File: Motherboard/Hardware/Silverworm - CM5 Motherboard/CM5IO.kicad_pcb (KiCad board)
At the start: 4 copper layers, 160 x 90 mm, 81 parts, among them J10 690-019-298-412, J11 USB_C_Receptacle_USB2.0, J12 USB3_A, J14 JST_SHBM04B-SRSS-TB, J16 Conn_01x22_Female, J2 Conn_02x07_Odd_Even, J22 690-019-298-412, J3 Conn_01x03, J4 Bus_M.2_Socket_M, J5 Conn_01x22_Female, J6 THD-02-R, J7 Micro_SD_Card_Det, J8 THD-20-R, J9 THD-02-R, SW1 Right angle Tact button, U1 TPD4EUSB30, U12 RT9742SNGV, U18 RT9742GGJ5, U2 TPD4EUSB30, U3 MagJack-A70-112-331N126, U6 AP22653W6, U7 ASEK-32.768KHZ-L-R-T, U8 AP3441SHE-7B

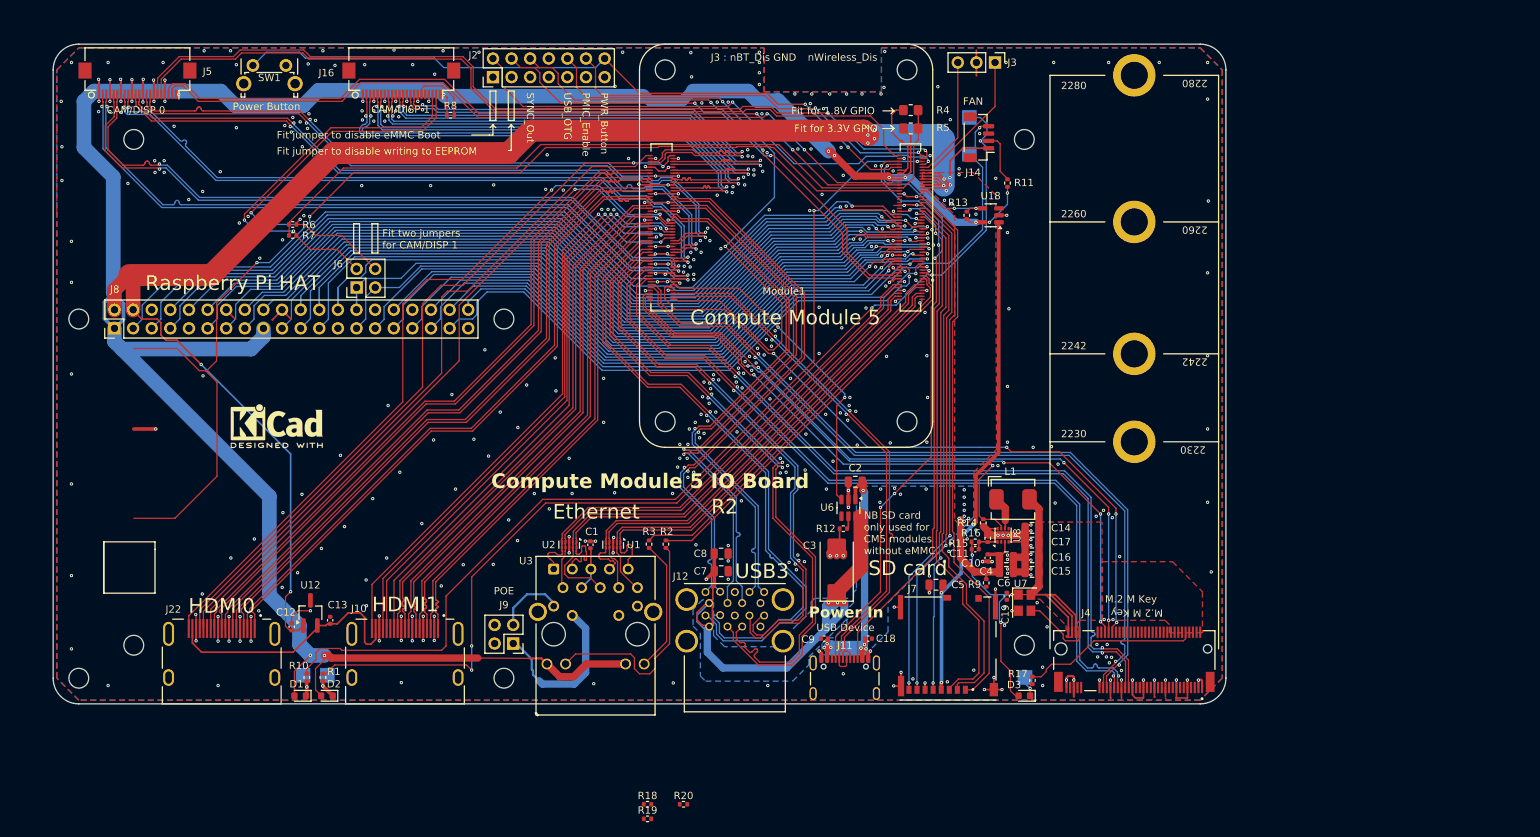
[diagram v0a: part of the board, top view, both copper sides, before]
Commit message: Added footprints and board connectors
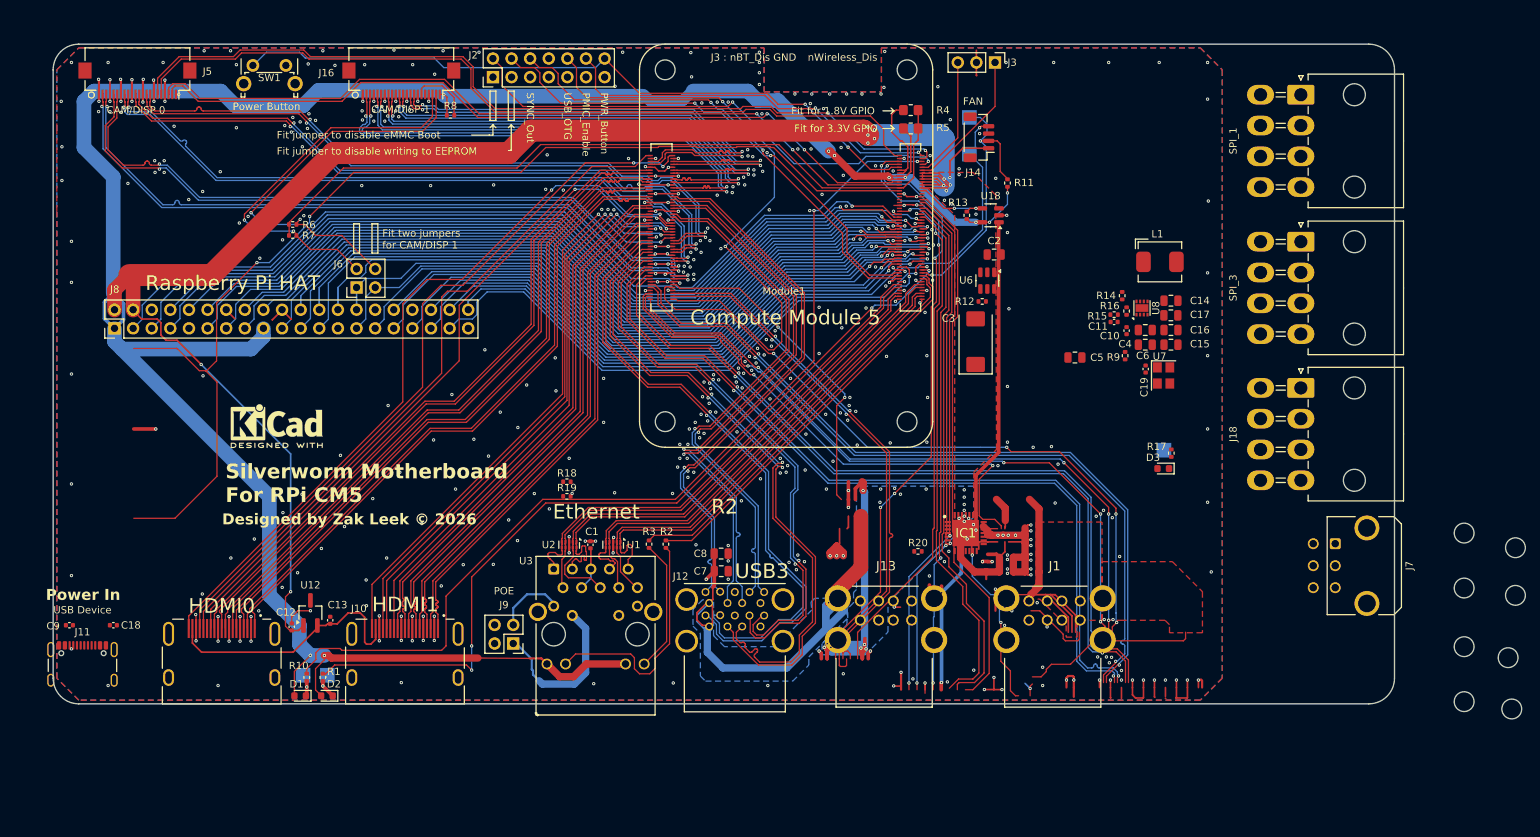
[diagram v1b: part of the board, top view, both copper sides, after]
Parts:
- removed J4: Bus_M.2_Socket_M, CM5IO:M.2 M Key socket
- added IC1: CY7C65632-28LTXC, CM5IO:QFN50P500X500X80-29N-D, F.Cu at (203.5, 136.7)
- added J1: USB_A_Stacked, CM5IO:57876171, F.Cu at (215.5, 152.2)
- added J13: USB_A_Stacked, CM5IO:57876171, F.Cu at (192.5, 152.2)
- added J18: Minifit 2x4, Connector_Molex:Molex_Mini-Fit_Jr_5569-08A2_2x04_P4.20mm_Horizontal, F.Cu at (249.2, 116.9)
- added SPI_1: Minifit 2x4, Connector_Molex:Molex_Mini-Fit_Jr_5569-08A2_2x04_P4.20mm_Horizontal, F.Cu at (249.2, 76.9)
- added SPI_3: Minifit 2x4, Connector_Molex:Molex_Mini-Fit_Jr_5569-08A2_2x04_P4.20mm_Horizontal, F.Cu at (249.2, 97.0)
- J7: value Micro_SD_Card_Det -> Microfit 6-pin; footprint CM5IO:SDCARD_MOLEX_503398-1892 -> Connector_Molex:Molex_Micro-Fit_3.0_43045-0621_2x03-1MP_P3.00mm_Horizontal
- moved H3 199.6 mm to (278.5, 145.2)
- moved H7 191.5 mm to (271.5, 144.2), turned to 90 degrees
- moved H2 190.0 mm to (271.5, 136.7), turned to 90 degrees
- moved H1 187.5 mm to (277.5, 153.7)
- moved H5 141.5 mm to (278.5, 138.7)
- moved H4 137.6 mm to (278.0, 160.7)
- moved J11 104.0 mm to (83.0, 155.7)
- moved C18 103.0 mm to (87.2, 149.3)
- moved C9 103.0 mm to (81.2, 149.3)
- moved H6 91.6 mm to (271.5, 152.2), turned to 90 degrees
- moved H8 60.5 mm to (271.5, 159.7), turned to 90 degrees
- moved J7 54.7 mm to (253.9, 138.2), turned to -90 degrees
- moved R20 47.0 mm to (197.0, 139.2)
- moved R18 45.4 mm to (149.1, 129.7)
- moved R19 45.4 mm to (149.1, 131.7)
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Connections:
- J7 pad 1: /CM5_GPIO ( Ethernet, GPIO, SDCARD)/SD_DAT2 -> GND
- J7 pad 2: /CM5_GPIO ( Ethernet, GPIO, SDCARD)/SD_DAT3 -> /CM5_GPIO ( Ethernet, GPIO, SDCARD)/5V0
- J7 pad 3: /CM5_GPIO ( Ethernet, GPIO, SDCARD)/SD_CMD -> /CM5_GPIO ( Ethernet, GPIO, SDCARD)/SCL
- J7 pad 4: /CM5_GPIO ( Ethernet, GPIO, SDCARD)/SD_PWR -> /CM5_GPIO ( Ethernet, GPIO, SDCARD)/SDA
- J7 pad 5: /CM5_GPIO ( Ethernet, GPIO, SDCARD)/SD_CLK -> /CM5_GPIO ( Ethernet, GPIO, SDCARD)/12VDC
- Module1 pad 102: /CM5_HighSpeed/PCIE_nCLKREQ -> unconnected-(Module1B-PCIe_nCLKREQ-Pad102)
- Module1 pad 104: /CM5_HighSpeed/PCIE_nWAKE -> unconnected-(Module1B-PCIE_nWAKE-Pad104)
- Module1 pad 106: /CM5_HighSpeed/PCIE_PWR_EN -> unconnected-(Module1B-PCIE_PWR_EN-Pad106)
- Module1 pad 109: /CM5_HighSpeed/PCIE_nRST -> unconnected-(Module1B-PCIe_nRST-Pad109)
- Module1 pad 110: /CM5_HighSpeed/PCIE_CLK_P -> unconnected-(Module1B-PCIe_CLK_P-Pad110)
- Module1 pad 112: /CM5_HighSpeed/PCIE_CLK_N -> unconnected-(Module1B-PCIe_CLK_N-Pad112)
- Module1 pad 116: /CM5_HighSpeed/PCIE_RX_P -> unconnected-(Module1B-PCIe_RX_P-Pad116)
- Module1 pad 118: /CM5_HighSpeed/PCIE_RX_N -> unconnected-(Module1B-PCIe_RX_N-Pad118)
- Module1 pad 122: /CM5_HighSpeed/PCIE_TX_P -> unconnected-(Module1B-PCIe_TX_P-Pad122)
- Module1 pad 124: /CM5_HighSpeed/PCIE_TX_N -> unconnected-(Module1B-PCIe_TX_N-Pad124)
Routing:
- net (no net): track 143.6 -> 0.00 mm, vias 4 -> 0
- net unconnected-(Module1B-PCIe_TX_N-Pad124): track 0.00 -> 109.5 mm, vias 0 -> 2
- net /CM5_HighSpeed/PCIE_TX_N: track 109.5 -> 0.00 mm, vias 2 -> 0
- net unconnected-(Module1B-PCIe_TX_P-Pad122): track 0.00 -> 109.5 mm, vias 0 -> 2
- net /CM5_HighSpeed/PCIE_TX_P: track 109.5 -> 0.00 mm, vias 2 -> 0
- net unconnected-(Module1B-PCIe_RX_N-Pad118): track 0.00 -> 107.9 mm, vias 0 -> 2
- net /CM5_HighSpeed/PCIE_RX_N: track 107.9 -> 0.00 mm, vias 2 -> 0
- net unconnected-(Module1B-PCIe_RX_P-Pad116): track 0.00 -> 107.8 mm, vias 0 -> 2
- net /CM5_HighSpeed/PCIE_RX_P: track 107.8 -> 0.00 mm, vias 2 -> 0
- net unconnected-(Module1B-PCIe_CLK_N-Pad112): track 0.00 -> 103.8 mm, vias 0 -> 2
- net /CM5_HighSpeed/PCIE_CLK_N: track 103.8 -> 0.00 mm, vias 2 -> 0
- net unconnected-(Module1B-PCIe_CLK_P-Pad110): track 0.00 -> 103.8 mm, vias 0 -> 2
- net /CM5_HighSpeed/PCIE_CLK_P: track 103.8 -> 0.00 mm, vias 2 -> 0
- net unconnected-(Module1B-PCIe_nRST-Pad109): track 0.00 -> 93.4 mm, vias 0 -> 4
- net /CM5_HighSpeed/PCIE_nRST: track 93.4 -> 0.00 mm, vias 4 -> 0
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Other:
- board size 160 x 90 mm -> 183 x 90 mm
- board text added: "Designed by Zak Leek © 2026"
- board text added: "Silverworm Motherboard For RPi CM5"
- board text added: "Why are you loking at my bottom? ;)"
- board text removed: "Compute Module 5 IO Board"
- board text removed: "M.2 M Key"
- board text removed: "NB SD card only used for CM5 modules without eMMC"
- board text removed: "SD card"

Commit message: Layout and IO edits
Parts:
- moved C10 21.4 mm to (224.1, 130.5)
- moved C11 21.4 mm to (222.4, 129.3)
- moved C14 21.4 mm to (230.2, 126.4)
- moved C15 21.4 mm to (230.2, 132.4)
- moved C16 21.4 mm to (230.2, 130.4)
- moved C17 21.4 mm to (230.1, 128.4)
- moved C19 21.4 mm to (226.7, 135.7)
- moved C4 21.4 mm to (226.7, 130.4)
- moved C5 21.4 mm to (217.1, 134.2)
- moved C6 21.4 mm to (226.7, 132.4)
- moved D3 21.4 mm to (229.1, 149.3)
- moved R14 21.4 mm to (223.5, 125.7)
- moved R15 21.4 mm to (222.4, 128.3)
- moved R9 21.4 mm to (223.9, 133.9)
- moved TP1 21.4 mm to (229.2, 146.8)
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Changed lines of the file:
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@@
 	(footprint "Capacitor_SMD:C_0805_2012Metric"
 		(layer "F.Cu")
-		(at 218.4 112.75 180)
+		(at 217.05 134.15 180)
 		(descr "Capacitor SMD 0805 (2012 Metric), square (rectangular) end terminal, IPC_7351 nominal, (Body size source: IPC-SM-782 page 76, https://www.pcb-3d.com/wordpress/wp-content/uploads/ipc-sm-782a_amendment_1_and_2.pdf, https://docs.google.com/spreadsheets/d/1BsfQQcO9C6DZCsRaXUlFlo91Tg2WpOkGARC1WS5S8t0/edit?usp=sharing), generated with kicad-footprint-generator")
 		(tags "capacitor")
@@
 	(footprint "LED_SMD:LED_0603_1608Metric"
 		(layer "F.Cu")
-		(at 230.45 127.9 180)
+		(at 229.1 149.3 180)
 		(descr "LED SMD 0603 (1608 Metric), square (rectangular) end terminal, IPC_7351 nominal, (Body size source: http://www.tortai-tech.com/upload/download/2011102023233369053.pdf), generated with kicad-footprint-generator")
 		(tags "LED")
@@
 	(footprint "Package_DFN_QFN:DFN-8-1EP_2x2mm_P0.5mm_EP1.05x1.75mm"
 		(layer "F.Cu")
-		(at 227.55 106 90)
+		(at 226.2 127.4 90)
 		(descr "DFN8 2x2, 0.5P; CASE 506CN (see ON Semiconductor 506CN.PDF)")
 		(tags "DFN 0.5")
@@
 	(footprint "Resistor_SMD:R_0402_1005Metric"
 		(layer "F.Cu")
-		(at 225.25 112.5 -90)
+		(at 223.9 133.9 -90)
 		(descr "Resistor SMD 0402 (1005 Metric), square (rectangular) end terminal, IPC_7351 nominal, (Body size source: IPC-SM-782 page 72, https://www.pcb-3d.com/wordpress/wp-content/uploads/ipc-sm-782a_amendment_1_and_2.pdf), generated with kicad-footprint-generator")
 		(tags "resistor")
@@
 	(footprint "Capacitor_SMD:C_0805_2012Metric"
 		(layer "F.Cu")
-		(at 228 111)
+		(at 226.65 132.4)
 		(descr "Capacitor SMD 0805 (2012 Metric), square (rectangular) end terminal, IPC_7351 nominal, (Body size source: IPC-SM-782 page 76, https://www.pcb-3d.com/wordpress/wp-content/uploads/ipc-sm-782a_amendment_1_and_2.pdf, https://docs.google.com/spreadsheets/d/1BsfQQcO9C6DZCsRaXUlFlo91Tg2WpOkGARC1WS5S8t0/edit?usp=sharing), generated with kicad-footprint-generator")
 		(tags "capacitor")
@@
 	(footprint "Capacitor_SMD:C_0805_2012Metric"
 		(layer "F.Cu")
-		(at 231.5 109 180)
+		(at 230.15 130.4 180)
 		(descr "Capacitor SMD 0805 (2012 Metric), square (rectangular) end terminal, IPC_7351 nominal, (Body size source: IPC-SM-782 page 76, https://www.pcb-3d.com/wordpress/wp-content/uploads/ipc-sm-782a_amendment_1_and_2.pdf, https://docs.google.com/spreadsheets/d/1BsfQQcO9C6DZCsRaXUlFlo91Tg2WpOkGARC1WS5S8t0/edit?usp=sharing), generated with kicad-footprint-generator")
 		(tags "capacitor")
@@
 	(footprint "Capacitor_SMD:C_0402_1005Metric"
 		(layer "F.Cu")
-		(at 225.45 109.085 -90)
+		(at 224.1 130.485 -90)
 		(descr "Capacitor SMD 0402 (1005 Metric), square (rectangular) end terminal, IPC_7351 nominal, (Body size source: IPC-SM-782 page 76, https://www.pcb-3d.com/wordpress/wp-content/uploads/ipc-sm-782a_amendment_1_and_2.pdf), generated with kicad-footprint-generator")
 		(tags "capacitor")
@@
 	(footprint "Capacitor_SMD:C_0402_1005Metric"
 		(layer "F.Cu")
-		(at 223.75 107.9)
+		(at 222.4 129.3)
 		(descr "Capacitor SMD 0402 (1005 Metric), square (rectangular) end terminal, IPC_7351 nominal, (Body size source: IPC-SM-782 page 76, https://www.pcb-3d.com/wordpress/wp-content/uploads/ipc-sm-782a_amendment_1_and_2.pdf), generated with kicad-footprint-generator")
 		(tags "capacitor")
@@
 	(footprint "Capacitor_SMD:C_0805_2012Metric"
 		(layer "F.Cu")
-		(at 231.4875 107 180)
+		(at 230.1375 128.4 180)
 		(descr "Capacitor SMD 0805 (2012 Metric), square (rectangular) end terminal, IPC_7351 nominal, (Body size source: IPC-SM-782 page 76, https://www.pcb-3d.com/wordpress/wp-content/uploads/ipc-sm-782a_amendment_1_and_2.pdf, https://docs.google.com/spreadsheets/d/1BsfQQcO9C6DZCsRaXUlFlo91Tg2WpOkGARC1WS5S8t0/edit?usp=sharing), generated with kicad-footprint-generator")
 		(tags "capacitor")
@@
 	(footprint "Crystal:Crystal_SMD_3225-4Pin_3.2x2.5mm"
 		(layer "F.Cu")
-		(at 230.5 115.2 -90)
+		(at 229.15 136.6 -90)
 		(descr "SMD Crystal SERIES SMD3225/4 http://www.txccrystal.com/images/pdf/7m-accuracy.pdf, 3.2x2.5mm^2 package")
 		(tags "SMD SMT crystal")
@@
 	(footprint "Resistor_SMD:R_0402_1005Metric"
 		(layer "F.Cu")
-		(at 231.55 125.8 90)
+		(at 230.2 147.2 90)
 		(descr "Resistor SMD 0402 (1005 Metric), square (rectangular) end terminal, IPC_7351 nominal, (Body size source: IPC-SM-782 page 72, https://www.pcb-3d.com/wordpress/wp-content/uploads/ipc-sm-782a_amendment_1_and_2.pdf), generated with kicad-footprint-generator")
 		(tags "resistor")
@@
 	(footprint "CM5IO:L_Bourns_SRP5030CC"
 		(layer "F.Cu")
-		(at 230 99.7)
+		(at 228.65 121.1)
 		(descr "Inductor, Bourns, SRP5030T, 5.7mmx5.2mm (Script generated with StandardBox.py) (https://www.bourns.com/data/global/pdfs/SRP5030T.pdf)")
 		(tags "Inductor Bourns_SRP5030T")
@@
 	(footprint "Resistor_SMD:R_0402_1005Metric"
 		(layer "F.Cu")
-		(at 225.45 106.415 90)
+		(at 224.1 127.815 90)
 		(descr "Resistor SMD 0402 (1005 Metric), square (rectangular) end terminal, IPC_7351 nominal, (Body size source: IPC-SM-782 page 72, https://www.pcb-3d.com/wordpress/wp-content/uploads/ipc-sm-782a_amendment_1_and_2.pdf), generated with kicad-footprint-generator")
 		(tags "resistor")
@@
 	(footprint "Resistor_SMD:R_0402_1005Metric"
 		(layer "F.Cu")
-		(at 223.75 106.9)
+		(at 222.4 128.3)
 		(descr "Resistor SMD 0402 (1005 Metric), square (rectangular) end terminal, IPC_7351 nominal, (Body size source: IPC-SM-782 page 72, https://www.pcb-3d.com/wordpress/wp-content/uploads/ipc-sm-782a_amendment_1_and_2.pdf), generated with kicad-footprint-generator")
 		(tags "resistor")
@@
 	(footprint "Capacitor_SMD:C_0805_2012Metric"
 		(layer "F.Cu")
-		(at 231.5 111 180)
+		(at 230.15 132.4 180)
 		(descr "Capacitor SMD 0805 (2012 Metric), square (rectangular) end terminal, IPC_7351 nominal, (Body size source: IPC-SM-782 page 76, https://www.pcb-3d.com/wordpress/wp-content/uploads/ipc-sm-782a_amendment_1_and_2.pdf, https://docs.google.com/spreadsheets/d/1BsfQQcO9C6DZCsRaXUlFlo91Tg2WpOkGARC1WS5S8t0/edit?usp=sharing), generated with kicad-footprint-generator")
 		(tags "capacitor")
@@
 	(footprint "Capacitor_SMD:C_0805_2012Metric"
 		(layer "F.Cu")
-		(at 231.5 105 180)
+		(at 230.15 126.4 180)
 		(descr "Capacitor SMD 0805 (2012 Metric), square (rectangular) end terminal, IPC_7351 nominal, (Body size source: IPC-SM-782 page 76, https://www.pcb-3d.com/wordpress/wp-content/uploads/ipc-sm-782a_amendment_1_and_2.pdf, https://docs.google.com/spreadsheets/d/1BsfQQcO9C6DZCsRaXUlFlo91Tg2WpOkGARC1WS5S8t0/edit?usp=sharing), generated with kicad-footprint-generator")
 		(tags "capacitor")
@@
 	(footprint "Resistor_SMD:R_0402_1005Metric"
 		(layer "F.Cu")
-		(at 224.85 104.315 -90)
+		(at 223.5 125.715 -90)
 		(descr "Resistor SMD 0402 (1005 Metric), square (rectangular) end terminal, IPC_7351 nominal, (Body size source: IPC-SM-782 page 72, https://www.pcb-3d.com/wordpress/wp-content/uploads/ipc-sm-782a_amendment_1_and_2.pdf), generated with kicad-footprint-generator")
 		(tags "resistor")
@@
 	(footprint "Capacitor_SMD:C_0805_2012Metric"
 		(layer "F.Cu")
-		(at 228 109)
+		(at 226.65 130.4)
 		(descr "Capacitor SMD 0805 (2012 Metric), square (rectangular) end terminal, IPC_7351 nominal, (Body size source: IPC-SM-782 page 76, https://www.pcb-3d.com/wordpress/wp-content/uploads/ipc-sm-782a_amendment_1_and_2.pdf, https://docs.google.com/spreadsheets/d/1BsfQQcO9C6DZCsRaXUlFlo91Tg2WpOkGARC1WS5S8t0/edit?usp=sharing), generated with kicad-footprint-generator")
 		(tags "capacitor")
@@
 	(footprint "Capacitor_SMD:C_0402_1005Metric"
 		(layer "F.Cu")
-		(at 228.05 114.32 -90)
+		(at 226.7 135.72 -90)
 		(descr "Capacitor SMD 0402 (1005 Metric), square (rectangular) end terminal, IPC_7351 nominal, (Body size source: IPC-SM-782 page 76, https://www.pcb-3d.com/wordpress/wp-content/uploads/ipc-sm-782a_amendment_1_and_2.pdf), generated with kicad-footprint-generator")
 		(tags "capacitor")
@@
 	(footprint "TestPoint:TestPoint_Pad_2.0x2.0mm"
 		(layer "B.Cu")
-		(at 230.55 125.4)
+		(at 229.2 146.8)
 		(descr "SMD rectangular pad as test Point, square 2.0mm side length")
 		(tags "test point SMD pad rectangle square")

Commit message: Updates
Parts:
- removed J18: Minifit 2x4, Connector_Molex:Molex_Mini-Fit_Jr_5569-08A2_2x04_P4.20mm_Horizontal
- added SPI_5: Minifit 2x4, Connector_Molex:Molex_Mini-Fit_Jr_5569-08A2_2x04_P4.20mm_Horizontal, F.Cu at (249.2, 116.9)
- R13: value 10K 1% -> 470R
- moved C18 155.2 mm to (242.4, 149.3)
- moved C9 155.2 mm to (236.4, 149.3)
- moved J11 155.2 mm to (238.2, 155.7)
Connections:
- Module1 pad 25: /CM5_GPIO ( Ethernet, GPIO, SDCARD)/GPIO21 -> /CM5_GPIO ( Ethernet, GPIO, SDCARD)/SCLK_1
- Module1 pad 26: /CM5_GPIO ( Ethernet, GPIO, SDCARD)/GPIO19 -> /CM5_GPIO ( Ethernet, GPIO, SDCARD)/MISO_1
- Module1 pad 27: /CM5_GPIO ( Ethernet, GPIO, SDCARD)/GPIO20 -> /CM5_GPIO ( Ethernet, GPIO, SDCARD)/MOSI_1
- Module1 pad 30: /CM5_GPIO ( Ethernet, GPIO, SDCARD)/GPIO6 -> /CM5_GPIO ( Ethernet, GPIO, SDCARD)/MOSI_3
- Module1 pad 34: /CM5_GPIO ( Ethernet, GPIO, SDCARD)/GPIO5 -> /CM5_GPIO ( Ethernet, GPIO, SDCARD)/MISO_3
- Module1 pad 37: /CM5_GPIO ( Ethernet, GPIO, SDCARD)/GPIO7 -> /CM5_GPIO ( Ethernet, GPIO, SDCARD)/SCLK_3
- Module1 pad 44: /CM5_GPIO ( Ethernet, GPIO, SDCARD)/GPIO10 -> /CM5_GPIO ( Ethernet, GPIO, SDCARD)/LK_1
- Module1 pad 46: /CM5_GPIO ( Ethernet, GPIO, SDCARD)/GPIO22 -> /CM5_GPIO ( Ethernet, GPIO, SDCARD)/LK_2
- Module1 pad 48: /CM5_GPIO ( Ethernet, GPIO, SDCARD)/GPIO27 -> /CM5_GPIO ( Ethernet, GPIO, SDCARD)/LK_3
- Module1 pad 49: /CM5_GPIO ( Ethernet, GPIO, SDCARD)/GPIO18 -> /CM5_GPIO ( Ethernet, GPIO, SDCARD)/CSn_1
- Module1 pad 50: /CM5_GPIO ( Ethernet, GPIO, SDCARD)/GPIO17 -> /CM5_GPIO ( Ethernet, GPIO, SDCARD)/LK_4
- Module1 pad 54: /CM5_GPIO ( Ethernet, GPIO, SDCARD)/GPIO4 -> /CM5_GPIO ( Ethernet, GPIO, SDCARD)/CSn_3
- Module1 pad 55: /CM5_GPIO ( Ethernet, GPIO, SDCARD)/GPIO14 -> /CM5_GPIO ( Ethernet, GPIO, SDCARD)/LED_DATA
- R13 pad 1: /+3.3v -> /CM5_GPIO ( Ethernet, GPIO, SDCARD)/LED_DATA
- R13 pad 2: /CM5_GPIO ( Ethernet, GPIO, SDCARD)/SD_PWR_ON -> Net-(J18-Pin_2)
- SPI_1 pad 1: unconnected-(SPI_1-Pin_1-Pad1) -> /CM5_GPIO ( Ethernet, GPIO, SDCARD)/MOSI_1
- SPI_1 pad 2: unconnected-(SPI_1-Pin_2-Pad2) -> /CM5_GPIO ( Ethernet, GPIO, SDCARD)/MISO_1
- SPI_1 pad 3: unconnected-(SPI_1-Pin_3-Pad3) -> /CM5_GPIO ( Ethernet, GPIO, SDCARD)/SCLK_1
- SPI_1 pad 4: unconnected-(SPI_1-Pin_4-Pad4) -> /CM5_GPIO ( Ethernet, GPIO, SDCARD)/CSn_1
- SPI_1 pad 5: unconnected-(SPI_1-Pin_5-Pad5) -> GND
- SPI_1 pad 6: unconnected-(SPI_1-Pin_6-Pad6) -> /CM5_GPIO ( Ethernet, GPIO, SDCARD)/12VDC
- SPI_1 pad 7: unconnected-(SPI_1-Pin_7-Pad7) -> /CM5_GPIO ( Ethernet, GPIO, SDCARD)/5V0
- SPI_1 pad 8: unconnected-(SPI_1-Pin_8-Pad8) -> GND
- SPI_3 pad 1: unconnected-(SPI_3-Pin_1-Pad1) -> /CM5_GPIO ( Ethernet, GPIO, SDCARD)/MOSI_3
- SPI_3 pad 2: unconnected-(SPI_3-Pin_2-Pad2) -> /CM5_GPIO ( Ethernet, GPIO, SDCARD)/MISO_3
- SPI_3 pad 3: unconnected-(SPI_3-Pin_3-Pad3) -> /CM5_GPIO ( Ethernet, GPIO, SDCARD)/SCLK_3
- SPI_3 pad 4: unconnected-(SPI_3-Pin_4-Pad4) -> /CM5_GPIO ( Ethernet, GPIO, SDCARD)/CSn_3
- SPI_3 pad 5: unconnected-(SPI_3-Pin_5-Pad5) -> GND
- SPI_3 pad 6: unconnected-(SPI_3-Pin_6-Pad6) -> /CM5_GPIO ( Ethernet, GPIO, SDCARD)/12VDC
- SPI_3 pad 7: unconnected-(SPI_3-Pin_7-Pad7) -> /CM5_GPIO ( Ethernet, GPIO, SDCARD)/5V0
- SPI_3 pad 8: unconnected-(SPI_3-Pin_8-Pad8) -> GND
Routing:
- net GND: track 764.8 -> 904.8 mm, vias 468 -> 476
- net /CM5_GPIO ( Ethernet, GPIO, SDCARD)/12VDC: track 0.00 -> 43.5 mm
- net /PCIe-M2/M2_3v3: track 70.4 -> 99.8 mm, vias 4 -> 6
- net Net-(IC1-DD-[3]): track 0.00 -> 22.5 mm, vias 0 -> 2
- net /CM5_GPIO ( Ethernet, GPIO, SDCARD)/5V0: track 0.00 -> 17.4 mm
- net /+5v: track 284.2 -> 298.7 mm
- net /CM5_HighSpeed/+5v: track 0.00 -> 10.9 mm, vias 0 -> 1
- net Net-(D3-K): track 2.72 -> 11.6 mm, vias 1 -> 2
- net Net-(U8-LX): track 4.52 -> 9.94 mm
- net Net-(J4-DAS/~{DSS}/~{LED1}): track 24.1 -> 29.0 mm
- net /PCIe-M2/FB: track 3.55 -> 7.12 mm
- net Net-(J11-D+-PadA6): track 0.00 -> 2.22 mm
- net Net-(J11-D--PadA7): track 0.00 -> 2.20 mm
- net /CM5_HighSpeed/HDMI_5v: track 33.6 -> 35.8 mm
- net /+3.3v: track 331.7 -> 333.7 mm
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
